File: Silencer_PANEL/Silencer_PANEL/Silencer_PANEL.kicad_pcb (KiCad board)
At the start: 2 copper layers, 50 x 200 mm, 20 parts

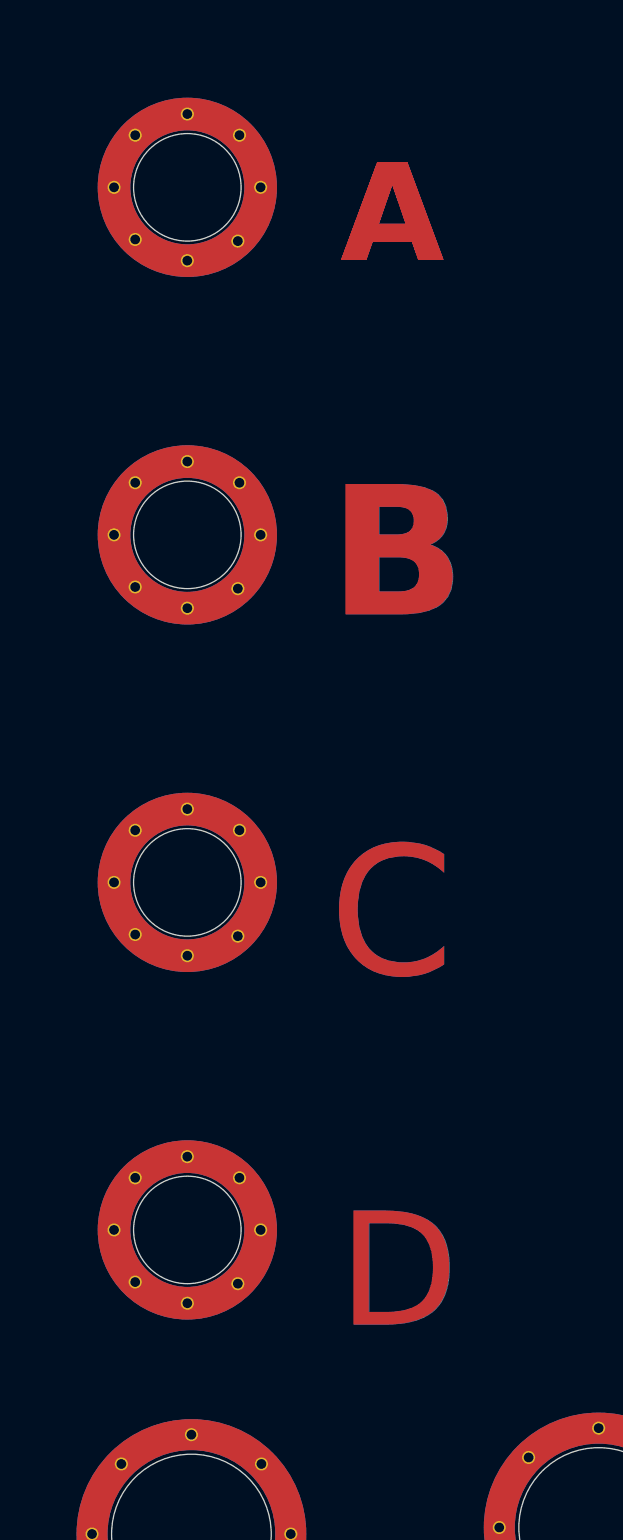
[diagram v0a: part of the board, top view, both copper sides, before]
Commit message: Top Board Layout lined up and routed.
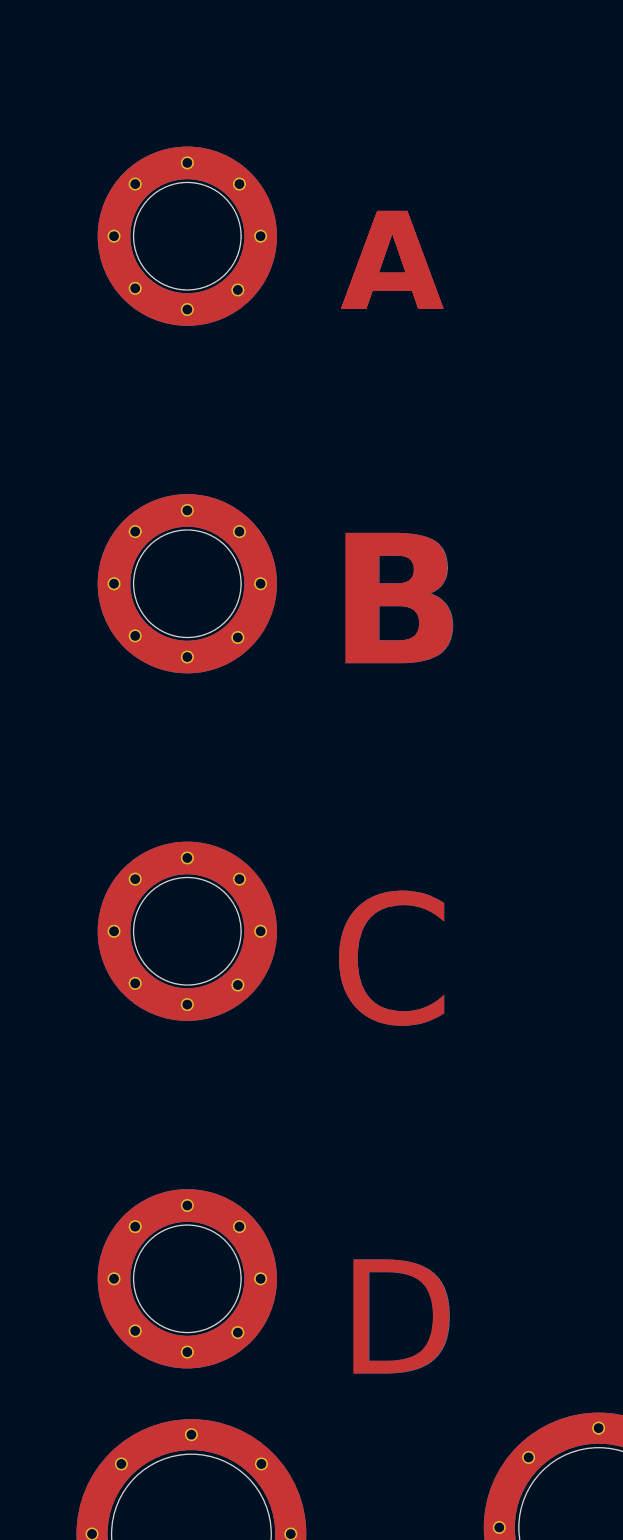
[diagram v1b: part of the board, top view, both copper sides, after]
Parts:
- moved REF** 3.00 mm to (12.2, 84.3)
- moved REF** 3.00 mm to (12.2, 63.0)
- moved REF** 3.00 mm to (12.2, 20.3)
- moved REF** 3.00 mm to (12.2, 41.7)
